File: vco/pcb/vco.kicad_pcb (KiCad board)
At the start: 2 copper layers, 50.5 x 108.5 mm, 98 parts, among them J1 Conn_02x05_Odd_Even, J10 AudioJack2_SwitchT, J2 AudioJack2_SwitchT, J3 AudioJack2_SwitchT, J4 AudioJack2_SwitchT, J5 AudioJack2_SwitchT, J6 AudioJack2_SwitchT, J7 AudioJack2_SwitchT, J8 AudioJack2_SwitchT, J9 AudioJack2_SwitchT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

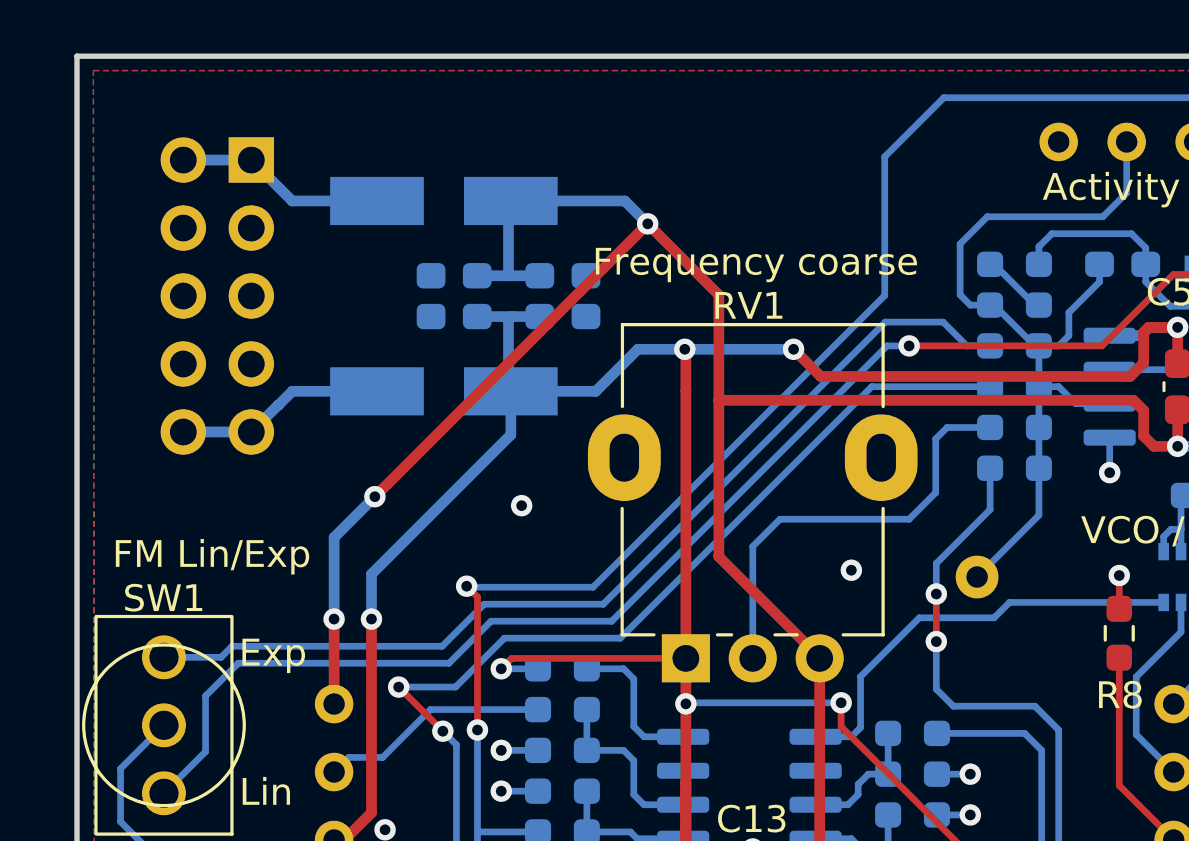
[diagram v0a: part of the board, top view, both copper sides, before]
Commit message: vco: Rotate the power connection on the pcb
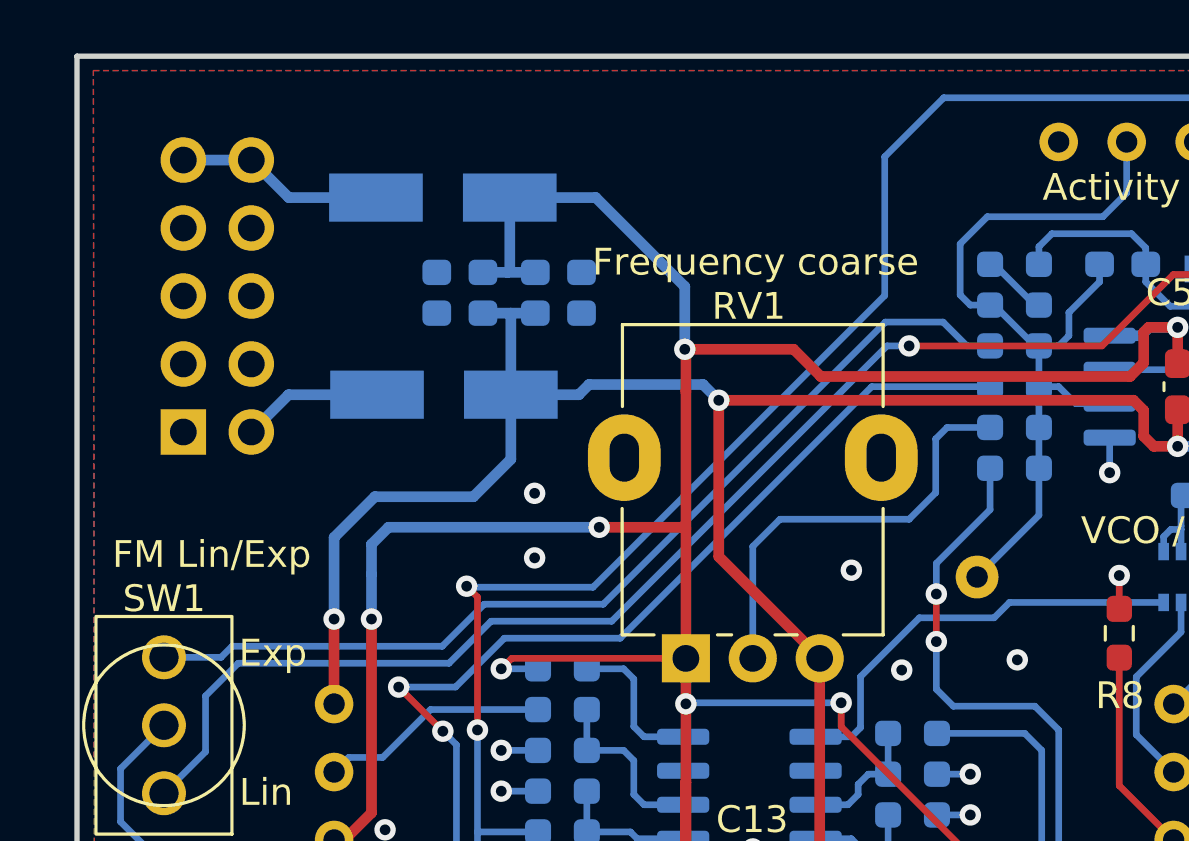
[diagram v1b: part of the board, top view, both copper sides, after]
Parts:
- moved J1 10.5 mm to (119.1, 65.5), turned to 0 degrees
- moved D1 7.24 mm to (128.8, 56.8)
- moved D2 7.24 mm to (128.8, 64.1)
- moved C3 1.66 mm to (129.4, 59.6)
- moved C1 1.66 mm to (133.1, 59.6)
- moved C4 1.41 mm to (129.4, 61.1)
- moved C2 1.41 mm to (133.1, 61.1)
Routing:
- net -12V: track 217.8 -> 206.5 mm, vias 12 -> 11
- net +12V: track 240.8 -> 247.7 mm
- net Net-(D2-Pad1): track 7.16 -> 5.27 mm
- net Net-(D1-Pad2): track 7.15 -> 7.78 mm
- net GND: vias 36 -> 39
